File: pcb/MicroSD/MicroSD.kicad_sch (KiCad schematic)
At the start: 9 parts, among them J1 Micro_SD_Card, J2 Conn_01x06_MountingPin, U1 74LVC125A, U2 AMS1117

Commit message: actualizacion esquematico
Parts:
- added FID1, FID2, FID3, FID4: Fiducial, Fiducial:Fiducial_1.5mm_Mask3mm, symbol Mechanical:Fiducial
- C1: footprint (none) -> Capacitor_THT:C_Axial_L5.1mm_D3.1mm_P10.00mm_Horizontal
- J1: footprint (none) -> Connector_Card:microSD_HC_Hirose_DM3D-SF
- J2: footprint (none) -> Connector_PinSocket_2.54mm:PinSocket_1x07_P2.54mm_Vertical
- R1, R2, R3, R4: footprint (none) -> Resistor_THT:R_Axial_DIN0309_L9.0mm_D3.2mm_P20.32mm_Horizontal
- U1: footprint 74LVC125APW_118:IC_74LVC125APW_118 -> Package_TO_SOT_SMD:SOT-1334-1
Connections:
- net VDD: now reaches C1.1, J1.4 (VDD), U1.14 (VCC), U2.2 (VO)
- net DAT3/CD: now reaches J1.2 (DAT3/CD), U1.8 (3Y)
- net PIN3: now reaches J2.3 (Pin_3), R4.2
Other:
- note added: "Buffer"
- note added: "Conector"
- note added: "Fiduciales"
- note added: "Regulador Voltaje"
- moved on the sheet: C1, J1, J2, R1, R2, R3, R4, U1, U2

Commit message: se agrega PCB
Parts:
- C1: footprint Capacitor_THT:C_Axial_L5.1mm_D3.1mm_P10.00mm_Horizontal -> Capacitor_SMD:C_1812_4532Metric
- R1, R2, R3, R4: footprint Resistor_THT:R_Axial_DIN0309_L9.0mm_D3.2mm_P20.32mm_Horizontal -> Resistor_SMD:R_0201_0603Metric
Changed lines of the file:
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@@
 			)
 		)
-		(property "Footprint" "Capacitor_THT:C_Axial_L5.1mm_D3.1mm_P10.00mm_Horizontal"
+		(property "Footprint" "Capacitor_SMD:C_1812_4532Metric"
 			(at 121.6152 90.17 0)
 			(effects
@@
 			)
 		)
-		(property "Footprint" "Resistor_THT:R_Axial_DIN0309_L9.0mm_D3.2mm_P20.32mm_Horizontal"
+		(property "Footprint" "Resistor_SMD:R_0201_0603Metric"
 			(at 102.87 113.538 90)
 			(effects
@@
 			)
 		)
-		(property "Footprint" "Resistor_THT:R_Axial_DIN0309_L9.0mm_D3.2mm_P20.32mm_Horizontal"
+		(property "Footprint" "Resistor_SMD:R_0201_0603Metric"
 			(at 177.8 136.398 90)
 			(effects
@@
 			)
 		)
-		(property "Footprint" "Resistor_THT:R_Axial_DIN0309_L9.0mm_D3.2mm_P20.32mm_Horizontal"
+		(property "Footprint" "Resistor_SMD:R_0201_0603Metric"
 			(at 102.87 128.778 90)
 			(effects
@@
 			)
 		)
-		(property "Footprint" "Resistor_THT:R_Axial_DIN0309_L9.0mm_D3.2mm_P20.32mm_Horizontal"
+		(property "Footprint" "Resistor_SMD:R_0201_0603Metric"
 			(at 102.87 121.158 90)
 			(effects

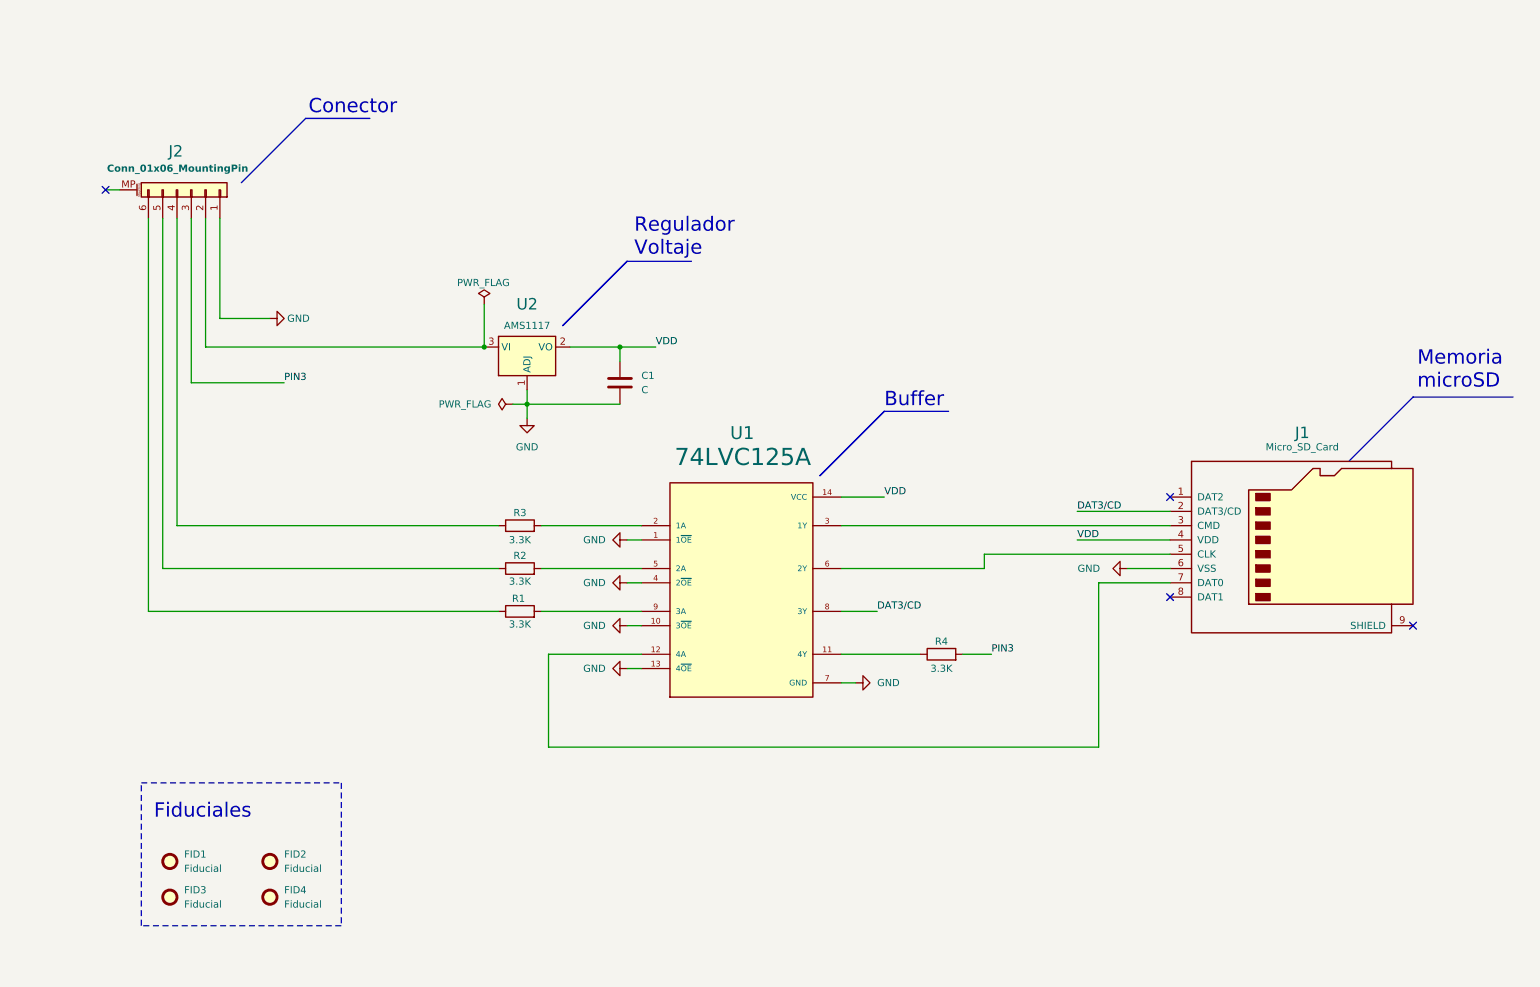
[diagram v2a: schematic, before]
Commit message: se agregan agujeros montaje
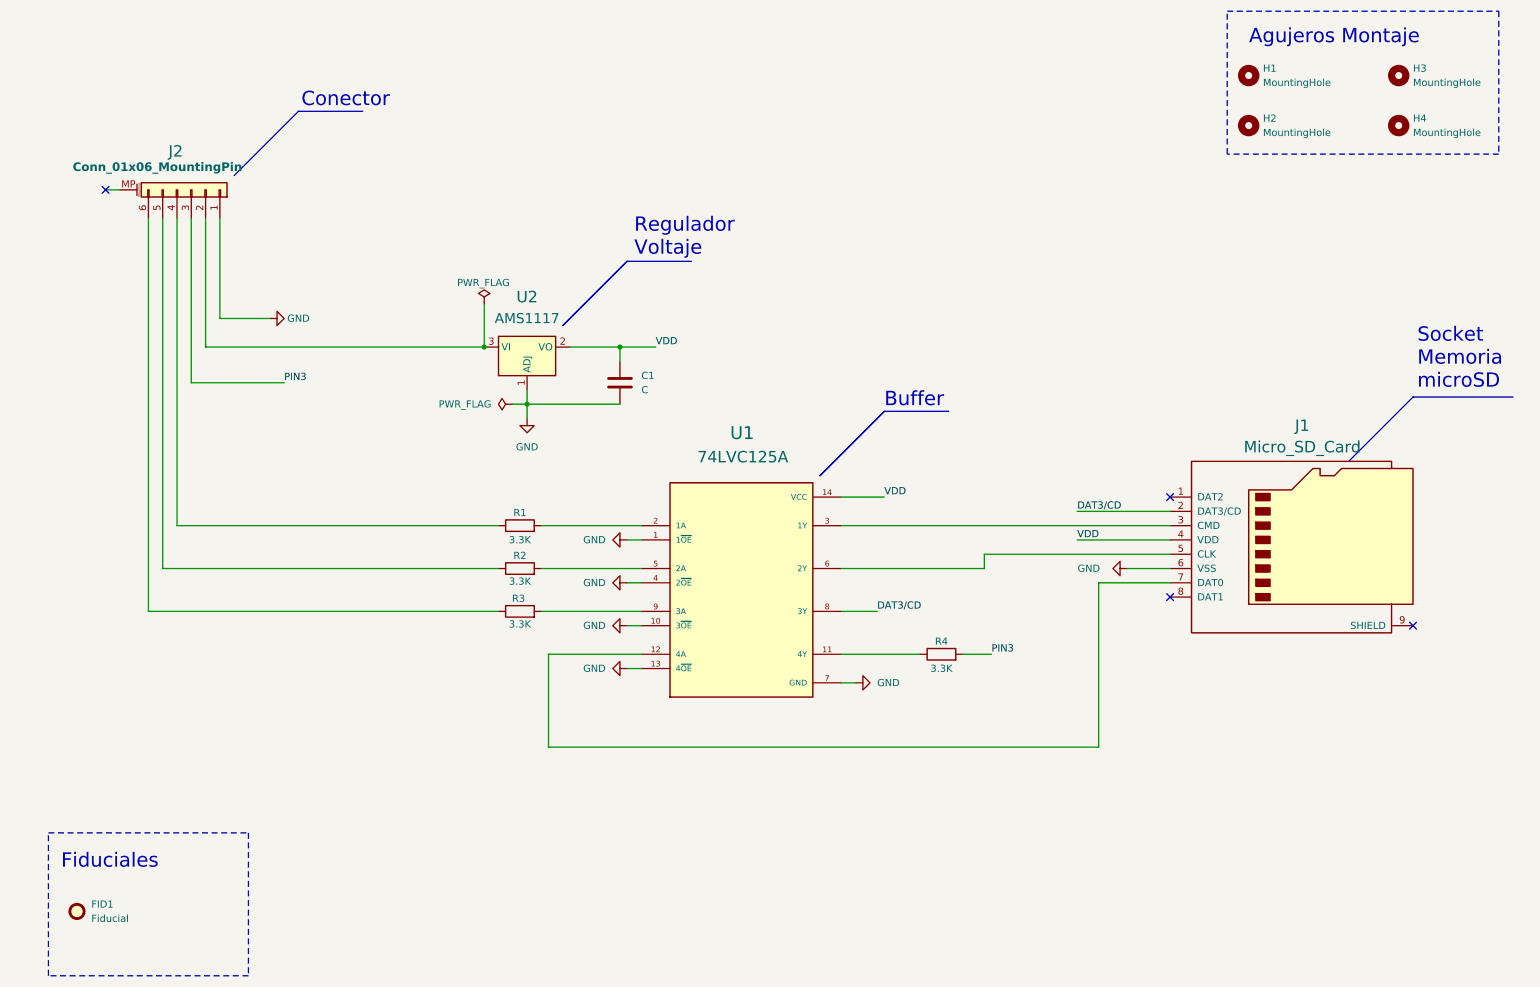
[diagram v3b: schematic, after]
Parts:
- removed FID2, FID3, FID4: Fiducial, Fiducial:Fiducial_1.5mm_Mask3mm, symbol Mechanical:Fiducial
- added H1, H2, H3, H4: MountingHole, MountingHole:MountingHole_3mm, symbol Mechanical:MountingHole
- renumbered R3 to R1, R1 to R3
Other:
- note added: "Agujeros Montaje"
- note added: "Socket Memoria microSD"
- note removed: "Memoria microSD"
- moved on the sheet: FID1

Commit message: se actualiza PCB y esquemas
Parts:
- removed U1: 74LVC125A, Package_TO_SOT_SMD:SOT-1334-1, symbol microUSB:74LVC125APW_118
- added U3: 74LVC125, Package_DIP:DIP-14_W7.62mm_SMDSocket_SmallPads, symbol 74xx:74LVC125
- H1, H2, H3, H4: footprint MountingHole:MountingHole_3mm -> MountingHole:MountingHole_2mm
- R1, R2, R3, R4: footprint Resistor_SMD:R_0201_0603Metric -> Resistor_SMD:R_0603_1608Metric
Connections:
- net DAT3/CD: now also U3.8
- net GND: now also U3.1, U3.10, U3.13, U3.4, U3.7 (GND)
- net VDD: now also U3.14 (VCC)
- net at R4.1: now also U3.11
- net at J1.7 (DAT0): now also U3.12
- net at R1.2: now also U3.2
- net at J1.3 (CMD): now also U3.3
- net at R2.2: now also U3.5
- net at J1.5 (CLK): now also U3.6
- net at R3.2: now also U3.9
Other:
- note added: "74LVC125"
- note removed: "Buffer"
- moved on the sheet: C1, R1, R2, R3, R4, U2

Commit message: se actualiza PCB y esquemas 2
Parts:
- C1: footprint Capacitor_SMD:C_1812_4532Metric -> Capacitor_SMD:C_1206_3216Metric_Pad1.33x1.80mm_HandSolder
- J1: footprint Connector_Card:microSD_HC_Hirose_DM3D-SF -> Connector_Card:microSD_HC_Wuerth_693072010801
- J2: footprint Connector_PinSocket_2.54mm:PinSocket_1x07_P2.54mm_Vertical -> Connector_Molex:Molex_PicoBlade_53398-0671_1x06-1MP_P1.25mm_Vertical
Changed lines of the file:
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@@
 			)
 		)
-		(property "Footprint" "Capacitor_SMD:C_1812_4532Metric"
+		(property "Footprint" "Capacitor_SMD:C_1206_3216Metric_Pad1.33x1.80mm_HandSolder"
 			(at 115.2652 73.66 0)
 			(effects
@@
 			)
 		)
-		(property "Footprint" "Connector_Card:microSD_HC_Hirose_DM3D-SF"
+		(property "Footprint" "Connector_Card:microSD_HC_Wuerth_693072010801"
 			(at 270.51 106.68 0)
 			(effects
@@
 			)
 		)
-		(property "Footprint" "Connector_PinSocket_2.54mm:PinSocket_1x07_P2.54mm_Vertical"
+		(property "Footprint" "Connector_Molex:Molex_PicoBlade_53398-0671_1x06-1MP_P1.25mm_Vertical"
 			(at 44.45 52.07 0)
 			(effects

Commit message: se actualiza resultados
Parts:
- added FID2: Fiducial, Fiducial:Fiducial_1.5mm_Mask3mm, symbol Mechanical:Fiducial
- J1: footprint Connector_Card:microSD_HC_Wuerth_693072010801 -> Connector_Card:microSD_HC_Hirose_DM3D-SF
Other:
- note added: "CLK"
- note added: "CS"
- note added: "GND"
- note added: "MISO"
- note added: "MOSI"
- note added: "VDD"
- title: Proyecto Final MicroUSB -> Réplica PCB de conector para microSD
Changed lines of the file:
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@@
 	(paper "A4")
 	(title_block
-		(title "Proyecto Final MicroUSB")
+		(title "Réplica PCB de conector para microSD")
 		(date "2024-09-01")
 		(rev "0.1")
 		(company "CESE")
 		(comment 1 "autor:  Luis Gómez")
-		(comment 2 "descripción: Esquemático memoria externa microSD")
+		(comment 2 "descripción: Esquemático para lector escritor de memoria externa microSD (réplica))")
+		(comment 3 "licencia: GPL")
 	)
 	(junction
@@
 		)
 	)
+	(text "VDD"
+		(exclude_from_sim no)
+		(at 45.974 58.166 90)
+		(effects
+			(font
+				(size 1.143 1.143)
+			)
+		)
+	)
+	(text "CLK"
+		(exclude_from_sim no)
+		(at 38.354 58.166 90)
+		(effects
+			(font
+				(size 1.143 1.143)
+			)
+		)
+	)
+	(text "MISO"
+		(exclude_from_sim no)
+		(at 43.434 58.42 90)
+		(effects
+			(font
+				(size 1.143 1.143)
+			)
+		)
+	)
 	(text "Fiduciales"
 		(exclude_from_sim no)
@@
 			)
 			(justify left)
+		)
+	)
+	(text "MOSI"
+		(exclude_from_sim no)
+		(at 40.894 58.42 90)
+		(effects
+			(font
+				(size 1.143 1.143)
+			)
+		)
+	)
+	(text "CS"
+		(exclude_from_sim no)
+		(at 36.068 57.658 90)
+		(effects
+			(font
+				(size 1.143 1.143)
+			)
+		)
+	)
+	(text "GND\n"
+		(exclude_from_sim no)
+		(at 48.514 58.166 90)
+		(effects
+			(font
+				(size 1.143 1.143)
+			)
 		)
 	)
@@
 	)
 	(symbol
+		(lib_id "Mechanical:Fiducial")
+		(at 40.64 180.34 0)
+		(unit 1)
+		(exclude_from_sim yes)
+		(in_bom no)
+		(on_board yes)
+		(dnp no)
+		(fields_autoplaced yes)
+		(property "Reference" "FID2"
+			(at 43.18 179.0699 0)
+			(effects
+				(font
+					(size 1.27 1.27)
+				)
+				(justify left)
+			)
+		)
+		(property "Value" "Fiducial"
+			(at 43.18 181.6099 0)
+			(effects
+				(font
+					(size 1.27 1.27)
+				)
+				(justify left)
+			)
+		)
+		(property "Footprint" "Fiducial:Fiducial_1.5mm_Mask3mm"
+			(at 40.64 180.34 0)
+			(effects
+				(font
+					(size 1.27 1.27)
+				)
+				(hide yes)
+			)
+		)
+		(property "Datasheet" "~"
+			(at 40.64 180.34 0)
+			(effects
+				(font
+					(size 1.27 1.27)
+				)
+				(hide yes)
+			)
+		)
+		(property "Description" "Fiducial Marker"
+			(at 40.64 180.34 0)
+			(effects
+				(font
+					(size 1.27 1.27)
+				)
+				(hide yes)
+			)
+		)
+		(instances
+			(project "MicroSD"
+				(path "/ead9c42e-d949-4523-ac5b-3e09aafd746b"
+					(reference "FID2")
+					(unit 1)
+				)
+			)
+		)
+	)
+	(symbol
 		(lib_id "Device:R")
 		(at 113.03 109.22 90)
@@
 			)
 		)
-		(property "Footprint" "Connector_Card:microSD_HC_Wuerth_693072010801"
+		(property "Footprint" "Connector_Card:microSD_HC_Hirose_DM3D-SF"
 			(at 270.51 106.68 0)
 			(effects

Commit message: README doc 18
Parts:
- C1: value C -> 100 nF
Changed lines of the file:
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@@
 		(comment 1 "autor:  Luis Gómez")
 		(comment 2 "descripción: Esquemático para lector escritor de memoria externa microSD (réplica))")
-		(comment 3 "licencia: GPL")
+		(comment 3 "licencia: GNU GENERAL PUBLIC LICENSE Version 3, 29 June 2007")
 	)
 	(junction
@@
 			)
 		)
-		(property "Value" "C"
+		(property "Value" "100 nF"
 			(at 118.11 71.1199 0)
-			(effects
-				(font
+			(do_not_autoplace yes)
+			(effects
+				(font
